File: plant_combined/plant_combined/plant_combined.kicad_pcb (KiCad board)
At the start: 4 copper layers, 88.9 x 58.4 mm, 72 parts, among them J1 SMA-J-P-H-ST-EM1, J2 PJ-002AH, J3 Conn_01x02, U1 SI5351A-B-GT, U10 ZXBM5210-SP-13, U2 OLED_DISP, U3 TDC7200PWR, U4 ADCMP600BKSZ-R2, U5 74AC14SC, U6 ESD7002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

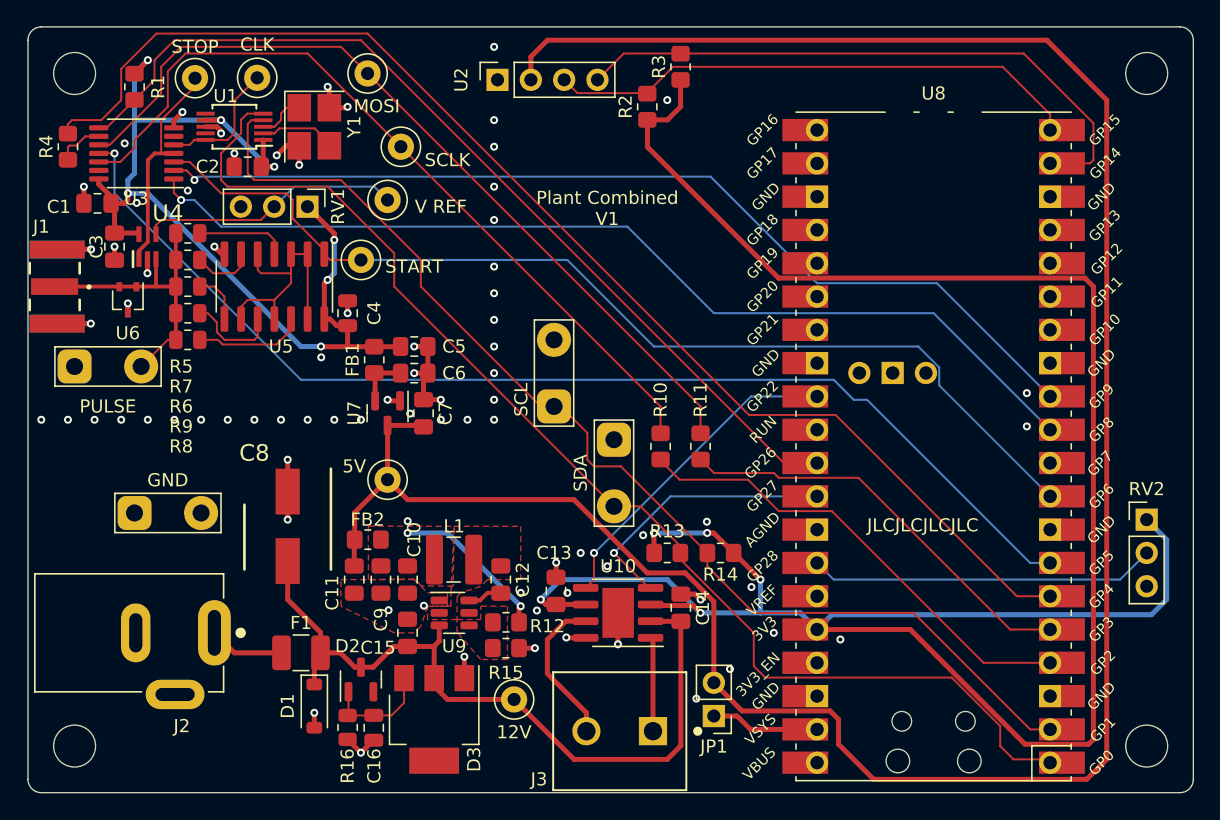
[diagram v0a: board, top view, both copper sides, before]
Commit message: Fixes for footprints
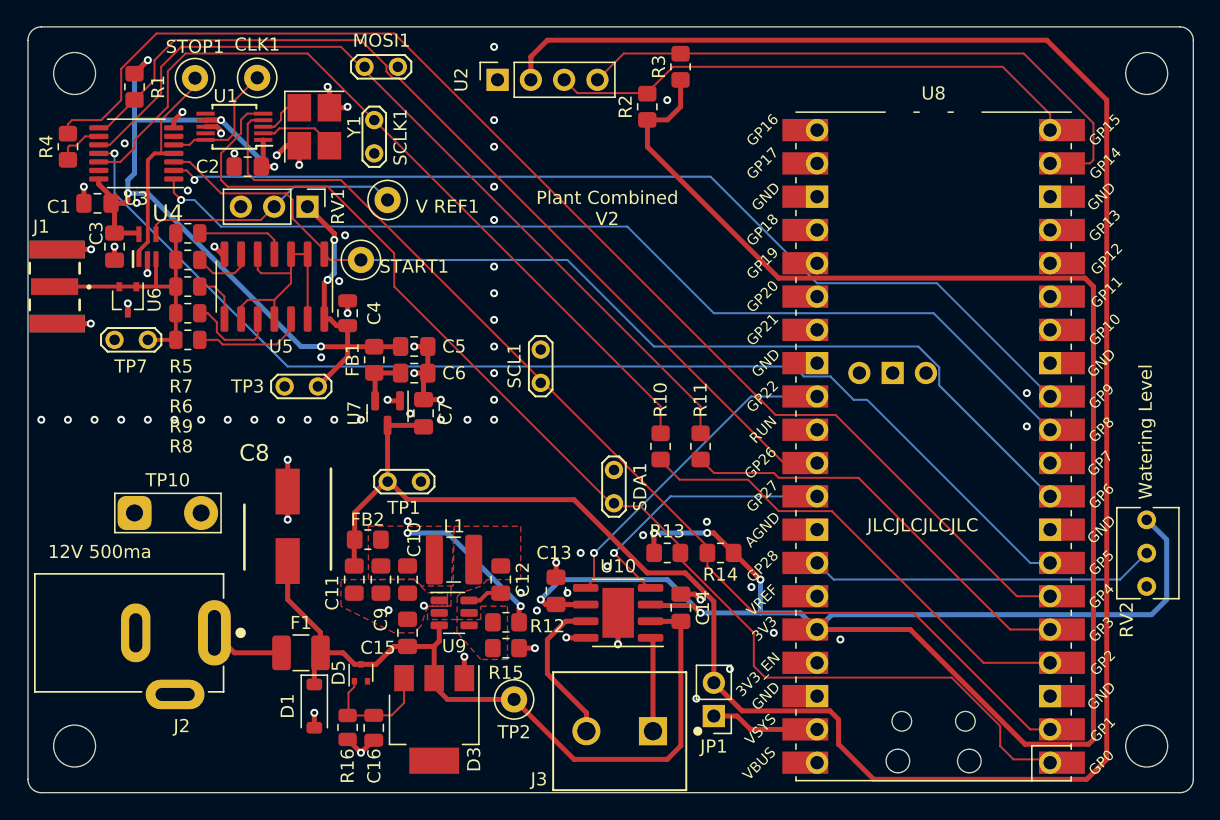
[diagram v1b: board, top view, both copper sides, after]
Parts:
- removed 5V, MOSI, SCLK: TestPoint, TestPoint:TestPoint_Loop_D1.80mm_Drill1.0mm_Beaded
- removed D2: BZX84C15T, Package_TO_SOT_SMD:SOT-23
- added D5: BZX84Cxx, Package_TO_SOT_SMD:SOT-523, F.Cu at (62.0, 114.3)
- added MOSI1: TestPoint, Library:TestPoint_2Pads_Pitch2.54mm_Drill1mm, F.Cu at (62.2, 68.1)
- added SCLK1: TestPoint, Library:TestPoint_2Pads_Pitch2.54mm_Drill1mm, F.Cu at (63.0, 72.1)
- added TP1: TestPoint, Library:TestPoint_2Pads_Pitch2.54mm_Drill1mm, F.Cu at (66.6, 99.7)
- added TP3: TestPoint_2Pole, Library:TestPoint_2Pads_Pitch2.54mm_Drill1mm, F.Cu at (56.2, 92.5)
- RV2: footprint Connector_PinHeader_2.54mm:PinHeader_1x03_P2.54mm_Vertical -> Potentiometer_THT:Potentiometer_Bourns_3266Y_Vertical
- SCL1: renamed from SCL; footprint TestPoint:TestPoint_2Pads_Pitch5.08mm_Drill1.3mm -> Library:TestPoint_2Pads_Pitch2.54mm_Drill1mm
- SDA1: renamed from SDA; footprint TestPoint:TestPoint_2Pads_Pitch5.08mm_Drill1.3mm -> Library:TestPoint_2Pads_Pitch2.54mm_Drill1mm
- TP7: renamed from PULSE; footprint TestPoint:TestPoint_2Pads_Pitch5.08mm_Drill1.3mm -> Library:TestPoint_2Pads_Pitch2.54mm_Drill1mm
- V REF1: renamed from V REF
- moved TP7 3.66 mm to (43.2, 88.9)
- moved SDA1 2.31 mm to (81.3, 98.8)
- moved SCL1 2.07 mm to (75.7, 92.2)
- turned RV2 to 90 degrees
- renumbered CLK to CLK1, START to START1, STOP to STOP1, GND to TP10, 12V to TP2
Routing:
- net +3.3VA: track 76.1 -> 80.0 mm
- net SCL: track 86.9 -> 84.8 mm
- net /tdr_sensor/PULSE: track 23.0 -> 21.6 mm
- net Net-(D3-G): track 8.43 -> 9.42 mm
- net GND: track 54.0 -> 53.6 mm, vias 79 -> 81
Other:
- board text added: "12V 500ma"
- board text added: "Plant Combined V2"
- board text added: "Watering Level"
- board text removed: "Plant Combined V1"
